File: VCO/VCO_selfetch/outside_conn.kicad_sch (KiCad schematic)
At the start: 3 parts

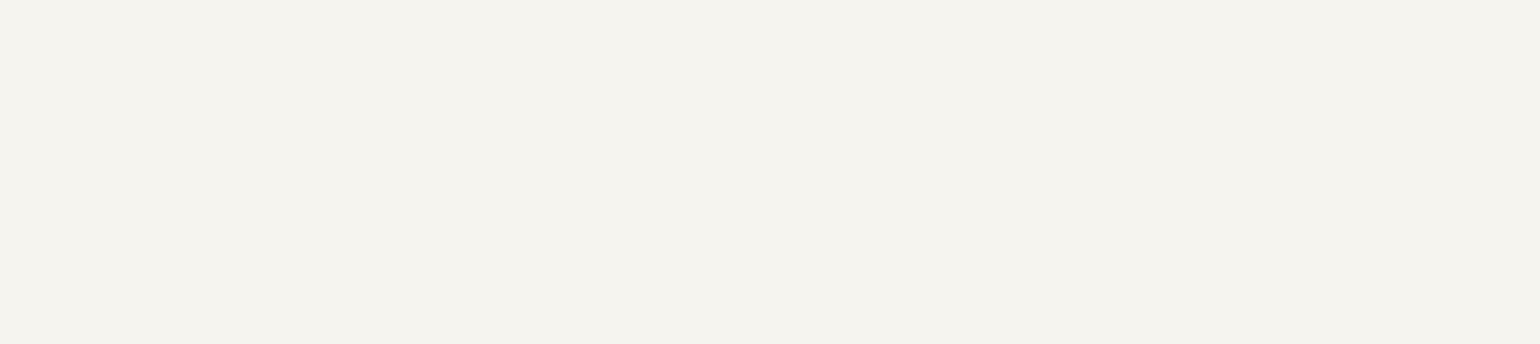
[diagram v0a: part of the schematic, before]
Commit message: added vco 2 and 3
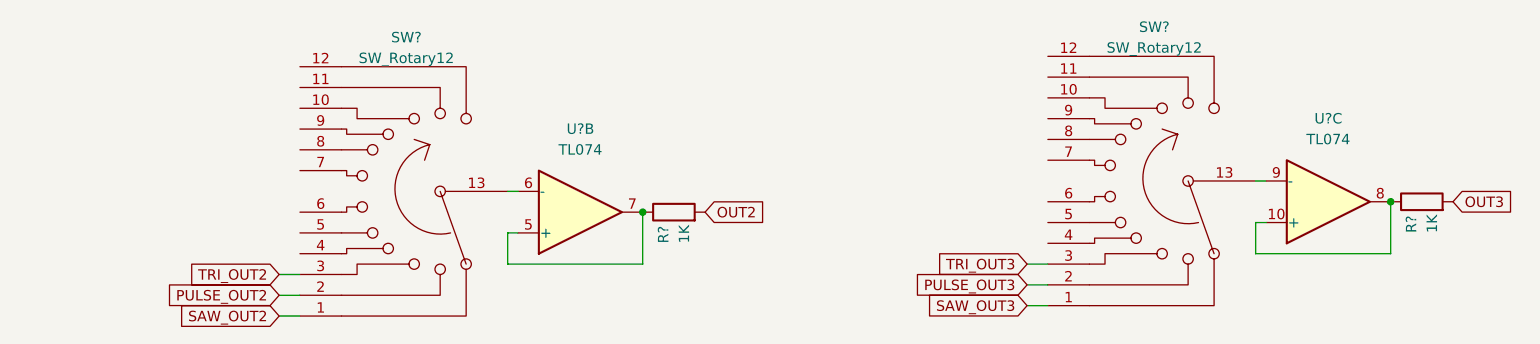
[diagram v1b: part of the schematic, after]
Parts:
- added R? (x2): 1K, symbol Device:R
- added SW? (x2): SW_Rotary12, symbol Switch:SW_Rotary12
- added U? (x2): TL074, symbol Amplifier_Operational:TL074
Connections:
- new net: R?.1, U?.10 (+), U?.8
- new net: R?.1, U?.5 (+), U?.7
- new net: SW?.13, U?.9 (-)
- new net: SW?.13, U?.6 (-)
- new net OUT2: R?.2
- new net OUT3: R?.2
- new net PULSE_OUT2: SW?.2
- new net PULSE_OUT3: SW?.2
- new net SAW_OUT2: SW?.1
- new net SAW_OUT3: SW?.1
- new net TRI_OUT2: SW?.3
- new net TRI_OUT3: SW?.3

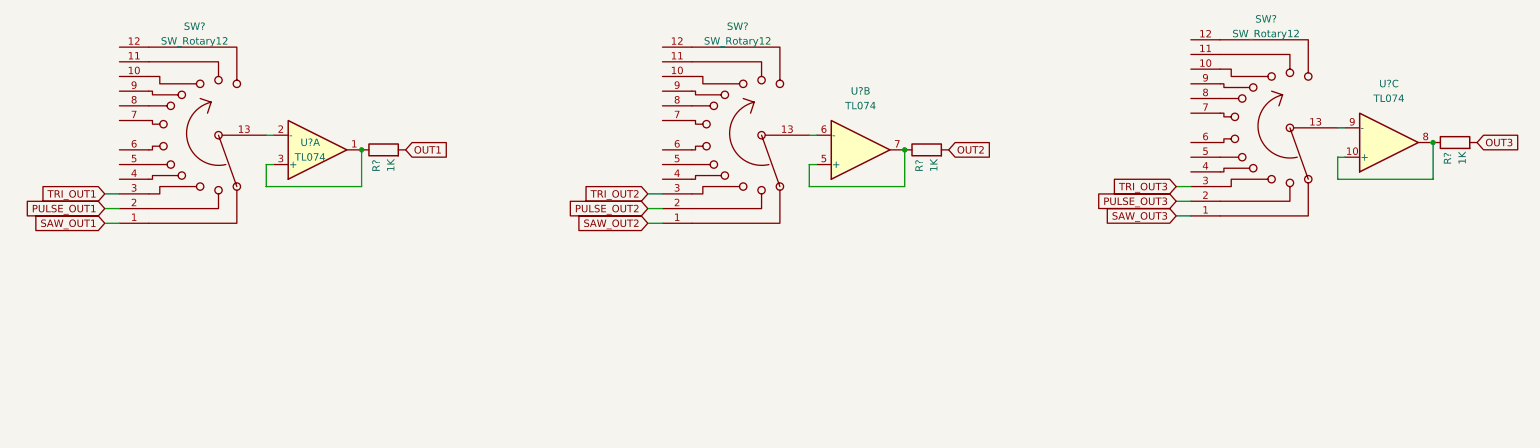
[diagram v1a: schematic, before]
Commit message: simple vco's added
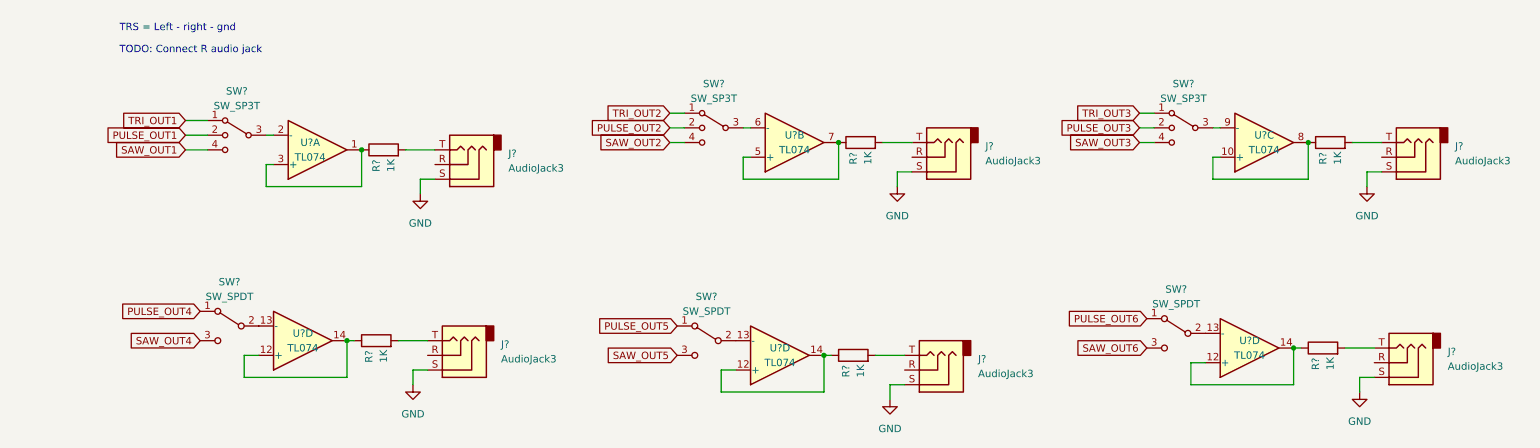
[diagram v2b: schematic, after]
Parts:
- removed SW? (x3): SW_Rotary12, symbol Switch:SW_Rotary12
- added J? (x6): AudioJack3, symbol Connector:AudioJack3
- added R? (x3): 1K, symbol Device:R
- added SW? (x3): SW_SP3T, symbol Switch:SW_SP3T
- added SW? (x3): SW_SPDT, symbol Switch:SW_SPDT
- added U? (x3): TL074, symbol Amplifier_Operational:TL074
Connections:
- net PULSE_OUT1: now also SW?.2
- net PULSE_OUT2: now also SW?.2
- net PULSE_OUT3: now also SW?.2
- net SAW_OUT1: now also SW?.4
- net SAW_OUT2: now also SW?.4
- net SAW_OUT3: now also SW?.4
- net TRI_OUT1: now also SW?.1
- net TRI_OUT2: now also SW?.1
- net TRI_OUT3: now also SW?.1
- net at U?.2 (-): now also SW?.3
- net at U?.9 (-): now also SW?.3
- net at U?.6 (-): now also SW?.3
- net OUT1: no longer names the net of R?.2
- net OUT1: now also J?.T
- net OUT2: no longer names the net of R?.2
- net OUT2: now also J?.T
- net OUT3: no longer names the net of R?.2
- net OUT3: now also J?.T
- new net: SW?.2 (B), U?.13 (-) (x3)
- new net: R?.1, U?.12 (+), U?.14 (x3)
- new net: J?.T, R?.2 (x3)
- new net GND: J?.S, J?.S, J?.S, J?.S, J?.S, J?.S
- new net PULSE_OUT4: SW?.1 (A)
- new net PULSE_OUT5: SW?.1 (A)
- new net PULSE_OUT6: SW?.1 (A)
- new net SAW_OUT4: SW?.3 (C)
- new net SAW_OUT5: SW?.3 (C)
- new net SAW_OUT6: SW?.3 (C)
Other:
- note added: "TODO: Connect R audio jack"
- note added: "TRS = Left - right - gnd"
- moved on the sheet: R?, U?B, U?C

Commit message: continue
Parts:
- added C? (x6): 1µ, symbol Device:C
- added D? (x6): 1N4148, Diode_THT:D_DO-35_SOD27_P7.62mm_Horizontal, symbol Diode:1N4148
- added Q1, Q11, Q3, Q5, Q7, Q9: NPN, symbol Simulation_SPICE:NPN
- added Q10, Q12, Q2, Q4, Q6, Q8: PNP, symbol Simulation_SPICE:PNP
- added R1, R11, R12, R14, R17, R18, R20, R23, R24, R26, R29, R30, R32, R35, R36, R4, R6, R8: 1K, symbol Device:R
- added R10, R16, R22, R28, R34, R5: 12K, symbol Device:R
- added R13, R19, R2, R25, R31, R7: 22K, symbol Device:R
- added R15, R21, R27, R3, R33, R9: 10K, symbol Device:R
- gave numbers to parts that had none: 21
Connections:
- net GND: now also C?.1, C?.1, C?.1, C?.1, C?.1, C?.1, R11.1, R13.1, R17.1, R19.1, R2.1, R23.1, R25.1, R29.1, R31.1, R35.1, R6.1, R7.1
- net OUT3: now reaches J6.T, R99.2
- net OUT3: now also D?.2 (A)
- net LED_OUT3: now reaches J6.R
- net LED_OUT3: now also Q5.3 (E), Q6.1 (C), R17.2
- net LED_OUT1: now reaches J2.R
- net LED_OUT1: now also Q1.3 (E), Q2.1 (C), R6.2
- net OUT1: now reaches J2.T, R95.2
- net OUT1: now also D?.2 (A)
- net OUT4: now reaches J1.T, R94.2
- net OUT4: now also D?.2 (A)
- net OUT2: now reaches J4.T, R97.2
- net OUT2: now also D?.2 (A)
- net OUT6: now reaches J5.T, R98.2
- net OUT6: now also D?.2 (A)
- net LED_OUT5: now reaches J3.R
- net LED_OUT5: now also Q10.1 (C), Q9.3 (E), R29.2
- net OUT5: now reaches J3.T, R96.2
- net OUT5: now also D?.2 (A)
- net LED_OUT4: now reaches J1.R
- net LED_OUT4: now also Q7.3 (E), Q8.1 (C), R23.2
- net LED_OUT6: now reaches J5.R
- net LED_OUT6: now also Q11.3 (E), Q12.1 (C), R35.2
- net LED_OUT2: now reaches J4.R
- net LED_OUT2: now also Q3.3 (E), Q4.1 (C), R11.2
- new net: D?.1 (K), R8.2, R9.2
- new net: Q7.1 (C), R22.2, R24.2
- new net: Q12.2 (B), R36.1
- new net: D?.1 (K), R20.2, R21.2
- new net: C?.2, R31.2, R32.1
- new net: D?.1 (K), R32.2, R33.2
- new net: C?.2, R7.2, R8.1
- new net: C?.2, R25.2, R26.1
- new net: D?.1 (K), R26.2, R27.2
- new net: Q1.1 (C), R4.2, R5.2
- new net: Q6.2 (B), R18.1
- new net: C?.2, R19.2, R20.1
- new net: Q4.2 (B), R12.1
- new net: Q11.2 (B), R33.1
- new net: Q9.1 (C), R28.2, R30.2
- new net: Q9.2 (B), R27.1
- new net: C?.2, R13.2, R14.1
- new net: D?.1 (K), R14.2, R15.2
- new net: Q8.2 (B), R24.1
- new net: Q5.2 (B), R15.1
- new net: Q5.1 (C), R16.2, R18.2
- new net: Q11.1 (C), R34.2, R36.2
- new net: Q10.2 (B), R30.1
- new net: Q1.2 (B), R3.1
- new net: D?.1 (K), R1.2, R3.2
- new net: C?.2, R1.1, R2.2
- new net: Q3.1 (C), R10.2, R12.2
- new net: Q3.2 (B), R9.1
- new net: Q7.2 (B), R21.1
- new net: Q2.2 (B), R4.1
- new net +12V: Q10.3 (E), Q12.3 (E), Q2.3 (E), Q4.3 (E), Q6.3 (E), Q8.3 (E), R10.1, R16.1, R22.1, R28.1, R34.1, R5.1
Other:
- note added: "BC807-40W AND BC817-40W"
- moved on the sheet: J1, J2, J3, J4, J5, J6, R94, R95, R96, R97, R98, R99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

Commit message: footprint WIP
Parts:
- removed Q1, Q11, Q3, Q5, Q7, Q9: NPN, symbol Simulation_SPICE:NPN
- removed Q10, Q12, Q2, Q4, Q6, Q8: PNP, symbol Simulation_SPICE:PNP
- added Q1, Q10, Q2, Q4, Q6, Q8: BC817, Package_TO_SOT_SMD:SOT-23, symbol Transistor_BJT:BC817
- added Q11, Q17, Q3, Q5, Q7, Q9: BC807, Package_TO_SOT_SMD:SOT-23, symbol Transistor_BJT:BC807
- C1, C2, C3, C4, C5, C6: renamed from C?; footprint (none) -> Capacitor_SMD:C_0402_1005Metric_Pad0.74x0.62mm_HandSolder
- D1, D2, D3, D4, D5, D6: renamed from D?; footprint Diode_THT:D_DO-35_SOD27_P7.62mm_Horizontal -> Diode_SMD:D_SOD-123
- J1, J2, J3, J4, J5, J6, SW1, SW3, SW5: footprint (none) -> Connector_PinHeader_2.54mm:PinHeader_1x03_P2.54mm_Vertical
- R1, R10, R11, R12, R13, R14, R15, R16, R17, R18, R19, R2, R20, R21, R22, R23, R24, R25, R26, R27, R28, R29, R3, R30, R31, R32, R33, R34, R35, R36, R4, R5, R6, R7, R8, R9, R94, R95, R96, R97, R98, R99: footprint (none) -> Resistor_SMD:R_0603_1608Metric_Pad0.98x0.95mm_HandSolder
- SW2, SW4, SW6: footprint (none) -> Connector_PinHeader_2.54mm:PinHeader_1x04_P2.54mm_Vertical
- U5, U6, U7: footprint (none) -> Package_DIP:DIP-14_W7.62mm_Socket
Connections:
- net +12V: now also Q11.2 (E), Q17.2 (E), Q3.2 (E), Q5.2 (E), Q7.2 (E), Q9.2 (E)
- net LED_OUT1: now also Q17.3 (C), Q2.2 (E)
- net LED_OUT2: now also J3.R, Q1.2 (E), Q3.3 (C); no longer J4.R
- net LED_OUT3: now also J5.R, Q4.2 (E), Q5.3 (C); no longer J6.R
- net LED_OUT4: now also Q6.2 (E), Q7.3 (C)
- net LED_OUT5: now also J4.R, Q8.2 (E), Q9.3 (C); no longer J3.R
- net LED_OUT6: now also J6.R, Q10.2 (E), Q11.3 (C); no longer J5.R
- net OUT2: now also J3.T; no longer J4.T
- net OUT3: now also J5.T; no longer J6.T
- net OUT5: now also J4.T; no longer J3.T
- net OUT6: now also J6.T; no longer J5.T
- net at R22.2, R24.2: now also Q6.3 (C)
- net at R36.1: now also Q11.1 (B)
- net at R4.2, R5.2: now also Q2.3 (C)
- net at R18.1: now also Q5.1 (B)
- net at R12.1: now also Q3.1 (B)
- net at R33.1: now also Q10.1 (B)
- net at R28.2, R30.2: now also Q8.3 (C)
- net at R27.1: now also Q8.1 (B)
- net at R24.1: now also Q7.1 (B)
- net at R15.1: now also Q4.1 (B)
- net at R16.2, R18.2: now also Q4.3 (C)
- net at R34.2, R36.2: now also Q10.3 (C)
- net at R30.1: now also Q9.1 (B)
- net at R3.1: now also Q2.1 (B)
- net at R10.2, R12.2: now also Q1.3 (C)
- net at R9.1: now also Q1.1 (B)
- net at R21.1: now also Q6.1 (B)
- net at R4.1: now also Q17.1 (B)

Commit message: all save
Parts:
- removed J1, J2, J3, J4, J5, J6: AudioJack3, Connector_PinHeader_2.54mm:PinHeader_1x03_P2.54mm_Vertical, symbol Connector:AudioJack3
- added C34, C35: 330uF, Capacitor_THT:CP_Radial_D12.5mm_P7.50mm, symbol Device:C_Polarized_Small_US
- added D19, D20: 1N4148, Diode_SMD:D_SOD-123, symbol Diode:1N4148
- added J1: Audiojack 2, Connector_PinHeader_2.54mm:PinHeader_1x03_P2.54mm_Vertical, symbol Connector:Conn_01x03_Socket
- added J2: Audiojack 3, Connector_PinHeader_2.54mm:PinHeader_1x03_P2.54mm_Vertical, symbol Connector:Conn_01x03_Socket
- added J3: Audiojack 4, Connector_PinHeader_2.54mm:PinHeader_1x03_P2.54mm_Vertical, symbol Connector:Conn_01x03_Socket
- added J4: Audiojack 5, Connector_PinHeader_2.54mm:PinHeader_1x03_P2.54mm_Vertical, symbol Connector:Conn_01x03_Socket
- added J5: Audiojack 6, Connector_PinHeader_2.54mm:PinHeader_1x03_P2.54mm_Vertical, symbol Connector:Conn_01x03_Socket
- added J7: Conn_02x08_Odd_Even, Connector_PinHeader_2.54mm:PinHeader_2x08_P2.54mm_Vertical, symbol Connector_Generic:Conn_02x08_Odd_Even
- added J8: Audiojack 1, Connector_PinHeader_2.54mm:PinHeader_1x03_P2.54mm_Vertical, symbol Connector:Conn_01x03_Socket
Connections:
- net +12V: now also C34.1, D19.1 (K)
- net GND: now also C34.2, C35.1, J1.3 (Pin_3), J2.3 (Pin_3), J3.3 (Pin_3), J4.3 (Pin_3), J5.3 (Pin_3), J7.10 (Pin_10), J7.11 (Pin_11), J7.12 (Pin_12), J7.13 (Pin_13), J7.14 (Pin_14), J7.9 (Pin_9), J8.3 (Pin_3)
- net LED_OUT1: now also J8.2 (Pin_2)
- net LED_OUT2: now also J1.2 (Pin_2)
- net LED_OUT3: now also J2.2 (Pin_2)
- net LED_OUT4: now also J3.2 (Pin_2)
- net LED_OUT5: now also J4.2 (Pin_2)
- net LED_OUT6: now also J5.2 (Pin_2)
- net OUT1: now also J8.1 (Pin_1)
- net OUT2: now also J1.1 (Pin_1)
- net OUT3: now also J2.1 (Pin_1)
- net OUT4: now also J3.1 (Pin_1)
- net OUT5: now also J4.1 (Pin_1)
- net OUT6: now also J5.1 (Pin_1)
- new net: D19.2 (A), J7.7 (Pin_7), J7.8 (Pin_8)
- new net: D20.1 (K), J7.15 (Pin_15), J7.16 (Pin_16)
- new net -12V: C35.2, D20.2 (A)
- no-connect marks 0 -> 6
